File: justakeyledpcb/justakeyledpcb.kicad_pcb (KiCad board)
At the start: 2 copper layers, 85.3 x 46 mm, 17 parts, among them SW1 SW_Push, SW2 SW_Push, SW3 SW_Push, SW4 SW_Push, U1 XIAO-RP2040-DIP

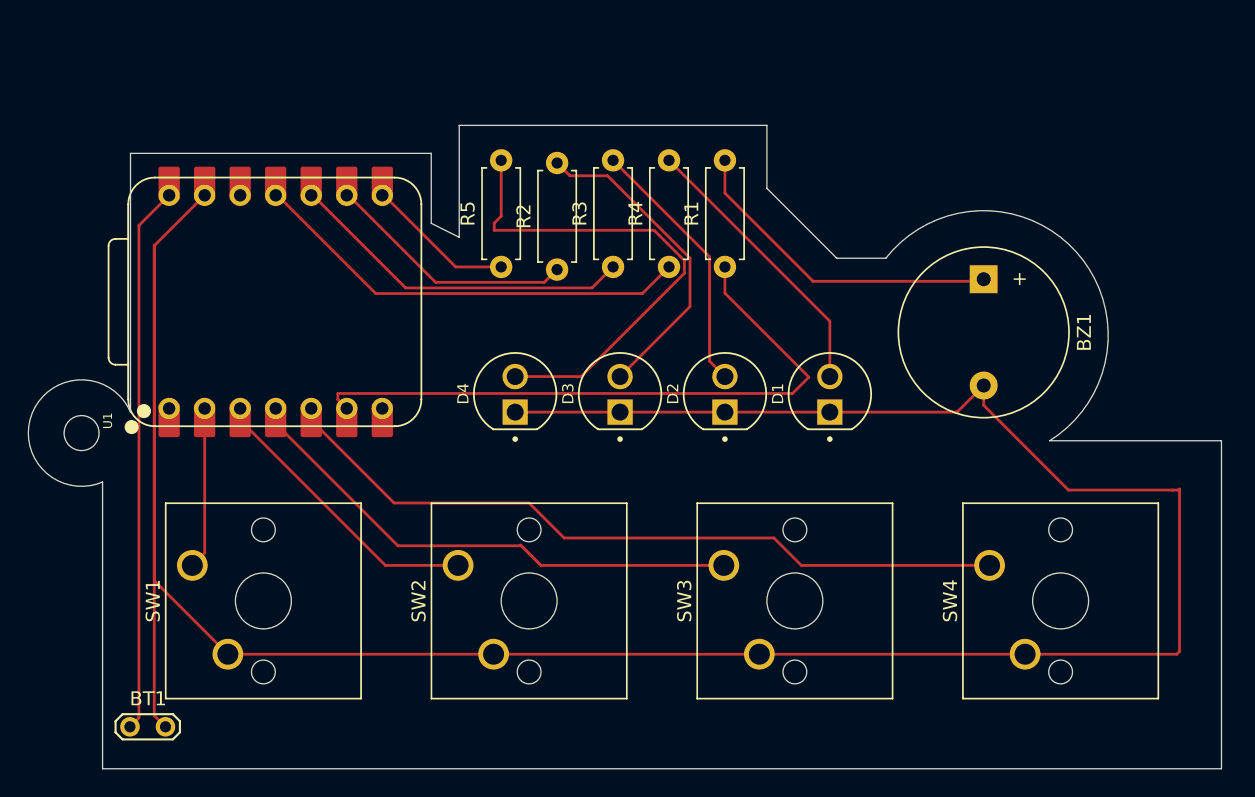
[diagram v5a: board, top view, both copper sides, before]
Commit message: Updated the Shape of the PCB
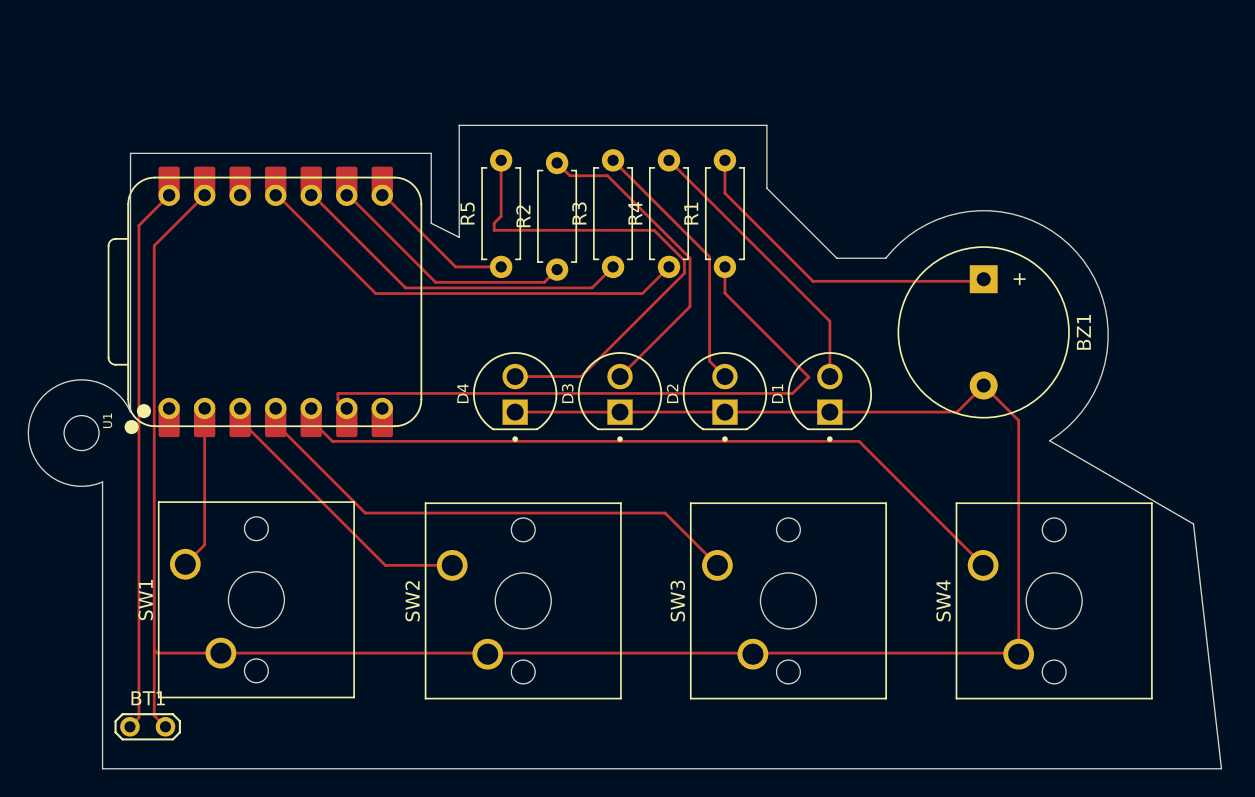
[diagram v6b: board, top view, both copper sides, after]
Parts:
- moved SW1 0.51 mm to (104.4, 70.4)
- moved SW3 0.46 mm to (142.5, 70.5)
- moved SW4 0.46 mm to (161.5, 70.5)
- moved SW2 0.42 mm to (123.5, 70.5)
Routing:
- net GND: track 203.2 -> 156.3 mm
- net Button 3: track 39.4 -> 36.9 mm
- net Button 1: track 12.4 -> 11.7 mm
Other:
- outline, holes or cut-outs redrawn
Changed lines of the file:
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@@
 	(footprint "Button_Switch_Keyboard:SW_Cherry_MX_1.00u_PCB"
 		(layer "F.Cu")
-		(at 142.92 70.46 90)
+		(at 142.46 70.46 90)
 		(descr "Cherry MX keyswitch, 1.00u, PCB mount, http://cherryamericas.com/wp-content/uploads/2014/12/mx_cat.pdf")
 		(tags "Cherry MX keyswitch 1.00u PCB")
@@
 	(footprint "Button_Switch_Keyboard:SW_Cherry_MX_1.00u_PCB"
 		(layer "F.Cu")
-		(at 123.92 70.46 90)
+		(at 123.5 70.46 90)
 		(descr "Cherry MX keyswitch, 1.00u, PCB mount, http://cherryamericas.com/wp-content/uploads/2014/12/mx_cat.pdf")
 		(tags "Cherry MX keyswitch 1.00u PCB")
@@
 	(footprint "Button_Switch_Keyboard:SW_Cherry_MX_1.00u_PCB"
 		(layer "F.Cu")
-		(at 104.92 70.46 90)
+		(at 104.42 70.38 90)
 		(descr "Cherry MX keyswitch, 1.00u, PCB mount, http://cherryamericas.com/wp-content/uploads/2014/12/mx_cat.pdf")
 		(tags "Cherry MX keyswitch 1.00u PCB")
@@
 	(footprint "Button_Switch_Keyboard:SW_Cherry_MX_1.00u_PCB"
 		(layer "F.Cu")
-		(at 161.92 70.46 90)
+		(at 161.46 70.46 90)
 		(descr "Cherry MX keyswitch, 1.00u, PCB mount, http://cherryamericas.com/wp-content/uploads/2014/12/mx_cat.pdf")
 		(tags "Cherry MX keyswitch 1.00u PCB")
@@
 	)
 	(gr_line
-		(start 166.21818 61.54909)
-		(end 178.5 61.54909)
-		(stroke
-			(width 0.05)
-			(type default)
-		)
-		(layer "Edge.Cuts")
-	)
-	(gr_line
 		(start 122 46)
 		(end 124 47)
@@
 	)
 	(gr_line
-		(start 178.5 85)
-		(end 98.5 85)
+		(start 166.218181 61.549089)
+		(end 176.5 67.5)
 		(stroke
 			(width 0.05)
@@
 	)
 	(gr_line
-		(start 146 43.5)
-		(end 151 48.5)
+		(start 176.5 67.5)
+		(end 178.5 85)
 		(stroke
 			(width 0.05)
@@
 	)
 	(gr_line
-		(start 100.5 59.500002)
-		(end 100.5 41)
+		(start 178.5 85)
+		(end 98.5 85)
 		(stroke
 			(width 0.05)
@@
 	)
 	(gr_line
-		(start 178.5 85)
-		(end 178.5 61.54909)
+		(start 146 43.5)
+		(end 151 48.5)
+		(stroke
+			(width 0.05)
+			(type default)
+		)
+		(layer "Edge.Cuts")
+	)
+	(gr_line
+		(start 100.5 59.500002)
+		(end 100.5 41)
 		(stroke
 			(width 0.05)
@@
 	)
 	(segment
-		(start 128 59.5)
-		(end 159.6 59.5)
+		(start 102.427 76.73)
+		(end 106.96 76.73)
 		(width 0.2)
 		(layer "F.Cu")
@@
 	)
 	(segment
-		(start 102.197 47.603)
-		(end 102.197 71.547)
-		(width 0.2)
-		(layer "F.Cu")
-		(net 2)
-	)
-	(segment
-		(start 102.197 47.603)
-		(end 105.8 44)
-		(width 0.2)
-		(layer "F.Cu")
-		(net 2)
-	)
-	(segment
-		(start 161.5 57.6)
-		(end 161.5 59.014213)
+		(start 128 59.5)
+		(end 159.6 59.5)
 		(width 0.2)
 		(layer "F.Cu")
@@
 	)
 	(segment
-		(start 159.6 59.5)
-		(end 161.5 57.6)
+		(start 164 76.81)
+		(end 164 60.1)
 		(width 0.2)
 		(layer "F.Cu")
@@
 	)
 	(segment
-		(start 175 65.075)
-		(end 175.425 65.075)
+		(start 163.92 76.73)
+		(end 164 76.81)
 		(width 0.2)
 		(layer "F.Cu")
@@
 	)
 	(segment
-		(start 175.425 65.075)
-		(end 175.5 65)
+		(start 102.197 47.603)
+		(end 105.8 44)
 		(width 0.2)
 		(layer "F.Cu")
@@
 	)
 	(segment
-		(start 167.560787 65.075)
-		(end 175 65.075)
+		(start 102.197 81.197)
+		(end 103 82)
 		(width 0.2)
 		(layer "F.Cu")
@@
 	)
 	(segment
-		(start 175.31 76.81)
-		(end 164.46 76.81)
+		(start 159.6 59.5)
+		(end 161.5 57.6)
 		(width 0.2)
 		(layer "F.Cu")
@@
 	)
 	(segment
-		(start 175.5 76.62)
-		(end 175.31 76.81)
+		(start 102.197 47.603)
+		(end 102.197 76.5)
 		(width 0.2)
 		(layer "F.Cu")
@@
 	)
 	(segment
-		(start 102.197 81.197)
-		(end 102.197 47.603)
+		(start 102.197 76.5)
+		(end 102.427 76.73)
 		(width 0.2)
 		(layer "F.Cu")
@@
 	)
 	(segment
-		(start 103 82)
+		(start 102.197 76.5)
 		(end 102.197 81.197)
 		(width 0.2)
@@
 	)
 	(segment
-		(start 175.5 65)
-		(end 175.5 76.62)
-		(width 0.2)
-		(layer "F.Cu")
-		(net 2)
-	)
-	(segment
-		(start 102.197 71.547)
-		(end 107.46 76.81)
-		(width 0.2)
-		(layer "F.Cu")
-		(net 2)
-	)
-	(segment
-		(start 107.46 76.81)
-		(end 164.46 76.81)
+		(start 164 60.1)
+		(end 161.5 57.6)
 		(width 0.2)
 		(layer "F.Cu")
@@
 	)
 	(segment
-		(start 161.5 59.014213)
-		(end 167.560787 65.075)
+		(start 106.96 76.73)
+		(end 163.92 76.73)
 		(width 0.2)
 		(layer "F.Cu")
@@
 	)
 	(segment
-		(start 105.8 69.58)
-		(end 104.92 70.46)
+		(start 105.8 60.075)
+		(end 105.8 59.24)
 		(width 0.2)
 		(layer "F.Cu")
@@
 	(segment
 		(start 105.8 60.075)
-		(end 105.8 59.24)
+		(end 105.8 69)
 		(width 0.2)
 		(layer "F.Cu")
@@
 	)
 	(segment
-		(start 105.8 59.24)
-		(end 105.8 69.58)
+		(start 105.8 69)
+		(end 104.42 70.38)
 		(width 0.2)
 		(layer "F.Cu")
@@
 	)
 	(segment
-		(start 108.34 60.075)
-		(end 118.725 70.46)
+		(start 118.725 70.46)
+		(end 123.5 70.46)
 		(width 0.2)
 		(layer "F.Cu")
@@
 	)
 	(segment
-		(start 118.725 70.46)
-		(end 123.92 70.46)
+		(start 108.34 60.075)
+		(end 118.725 70.46)
 		(width 0.2)
 		(layer "F.Cu")
@@
 	)
 	(segment
-		(start 119.62137 69.059)
-		(end 128.44053 69.059)
+		(start 117.28137 66.719)
+		(end 138.719 66.719)
 		(width 0.2)
 		(layer "F.Cu")
@@
 	)
 	(segment
-		(start 128.44053 69.059)
-		(end 129.84153 70.46)
+		(start 110.88 60.31763)
+		(end 117.28137 66.719)
 		(width 0.2)
 		(layer "F.Cu")
@@
 	)
 	(segment
-		(start 129.84153 70.46)
-		(end 142.92 70.46)
-		(width 0.2)
-		(layer "F.Cu")
-		(net 14)
-	)
-	(segment
-		(start 110.88 60.31763)
-		(end 119.62137 69.059)
-		(width 0.2)
-		(layer "F.Cu")
-		(net 14)
-	)
-	(segment
-		(start 128.38153 69)
-		(end 129.84153 70.46)
+		(start 138.719 66.719)
+		(end 142.46 70.46)
 		(width 0.2)
 		(layer "F.Cu")
@@
 	(segment
 		(start 113.42 60.075)
-		(end 119.345 66)
-		(width 0.2)
-		(layer "F.Cu")
-		(net 15)
-	)
-	(segment
-		(start 119.345 66)
-		(end 129 66)
-		(width 0.2)
-		(layer "F.Cu")
-		(net 15)
-	)
-	(segment
-		(start 148.46 70.46)
-		(end 161.92 70.46)
-		(width 0.2)
-		(layer "F.Cu")
-		(net 15)
-	)
-	(segment
-		(start 129 66)
-		(end 131.5 68.5)
+		(end 114.937 61.592)
 		(width 0.2)
 		(layer "F.Cu")
@@
 	)
 	(segment
-		(start 131.5 68.5)
-		(end 146.5 68.5)
+		(start 114.937 61.592)
+		(end 152.592 61.592)
 		(width 0.2)
 		(layer "F.Cu")
@@
 	)
 	(segment
-		(start 146.5 68.5)
-		(end 148.46 70.46)
+		(start 152.592 61.592)
+		(end 161.46 70.46)
 		(width 0.2)
 		(layer "F.Cu")

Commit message: had fun with the beizure curve thingy
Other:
- board size 85.3 x 46 mm -> 85.7 x 52.9 mm
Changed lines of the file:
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@@
 	)
 	(gr_line
-		(start 146 39)
-		(end 146 43.5)
-		(stroke
-			(width 0.05)
-			(type default)
-		)
-		(layer "Edge.Cuts")
-	)
-	(gr_line
-		(start 124 47)
-		(end 124 39)
+		(start 166.21818 61.54909)
+		(end 174.5 61.54909)
 		(stroke
 			(width 0.05)
@@
 	)
 	(gr_line
-		(start 100.5 41)
-		(end 122 41)
-		(stroke
-			(width 0.05)
-			(type default)
-		)
-		(layer "Edge.Cuts")
-	)
-	(gr_line
 		(start 98.5 64.499999)
 		(end 98.5 85)
@@
 	)
 	(gr_line
-		(start 124 39)
-		(end 146 39)
+		(start 98.5 85)
+		(end 172.5 85)
 		(stroke
 			(width 0.05)
@@
 		(layer "Edge.Cuts")
 	)
-	(gr_line
-		(start 166.218181 61.549089)
-		(end 176.5 67.5)
+	(gr_curve
+		(pts
+			(xy 174.5 61.54909) (xy 178.5 61.54909) (xy 178.5 66.5) (xy 178.5 66.5)
+		)
 		(stroke
 			(width 0.05)
@@
 		(layer "Edge.Cuts")
 	)
-	(gr_line
-		(start 176.5 67.5)
-		(end 178.5 85)
-		(stroke
-			(width 0.05)
-			(type default)
+	(gr_curve
+		(pts
+			(xy 124 47) (xy 128.5 12.5) (xy 151 48.5) (xy 151 48.5)
 		)
-		(layer "Edge.Cuts")
-	)
-	(gr_line
-		(start 178.5 85)
-		(end 98.5 85)
-		(stroke
-			(width 0.05)
-			(type default)
-		)
-		(layer "Edge.Cuts")
-	)
-	(gr_line
-		(start 146 43.5)
-		(end 151 48.5)
 		(stroke
 			(width 0.05)
@@
 		(stroke
 			(width 0.05)
+			(type default)
+		)
+		(layer "Edge.Cuts")
+	)
+	(gr_curve
+		(pts
+			(xy 100.5 41) (xy 81.5 37.5) (xy 122 30) (xy 122 41)
+		)
+		(stroke
+			(width 0.05)
+			(type default)
+		)
+		(layer "Edge.Cuts")
+	)
+	(gr_curve
+		(pts
+			(xy 172.5 85) (xy 181 85) (xy 178.5 66.5) (xy 178.5 66.5)
+		)
+		(stroke
+			(width 0.05)

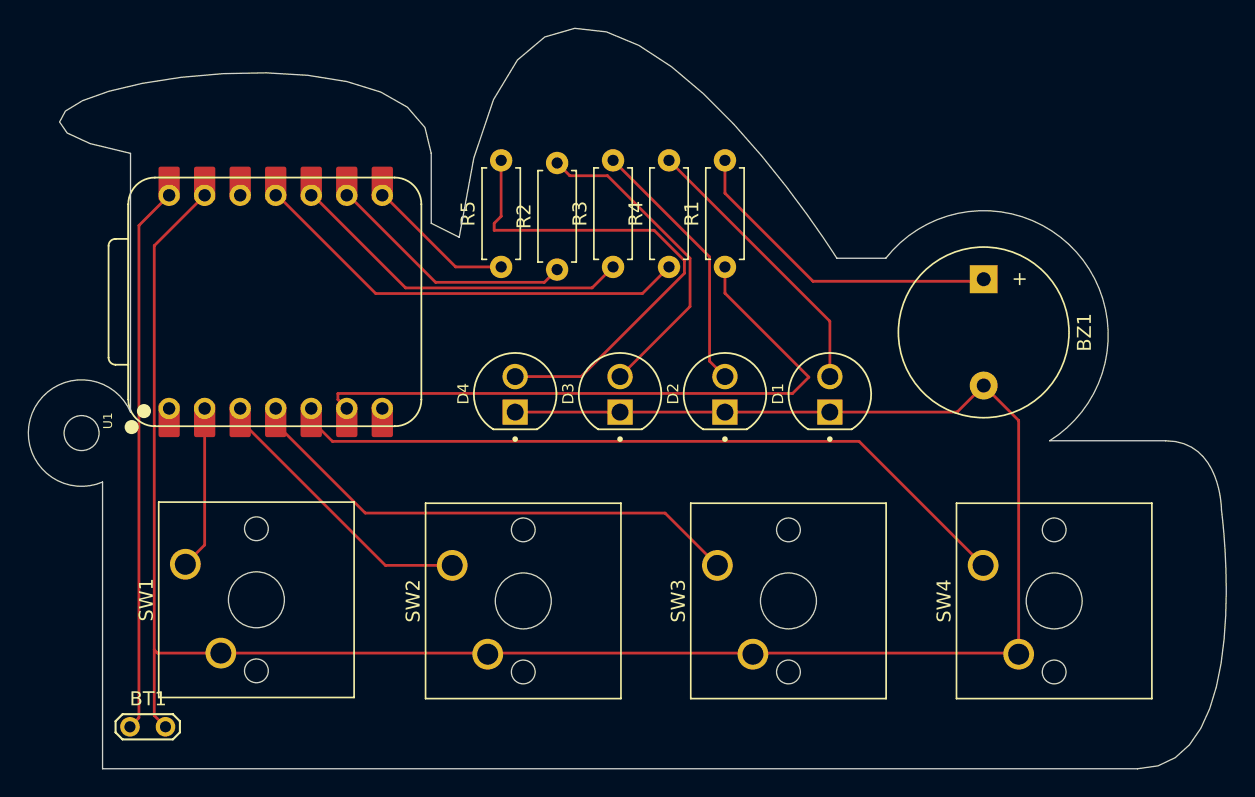
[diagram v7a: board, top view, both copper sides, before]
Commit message: added the silkscreen
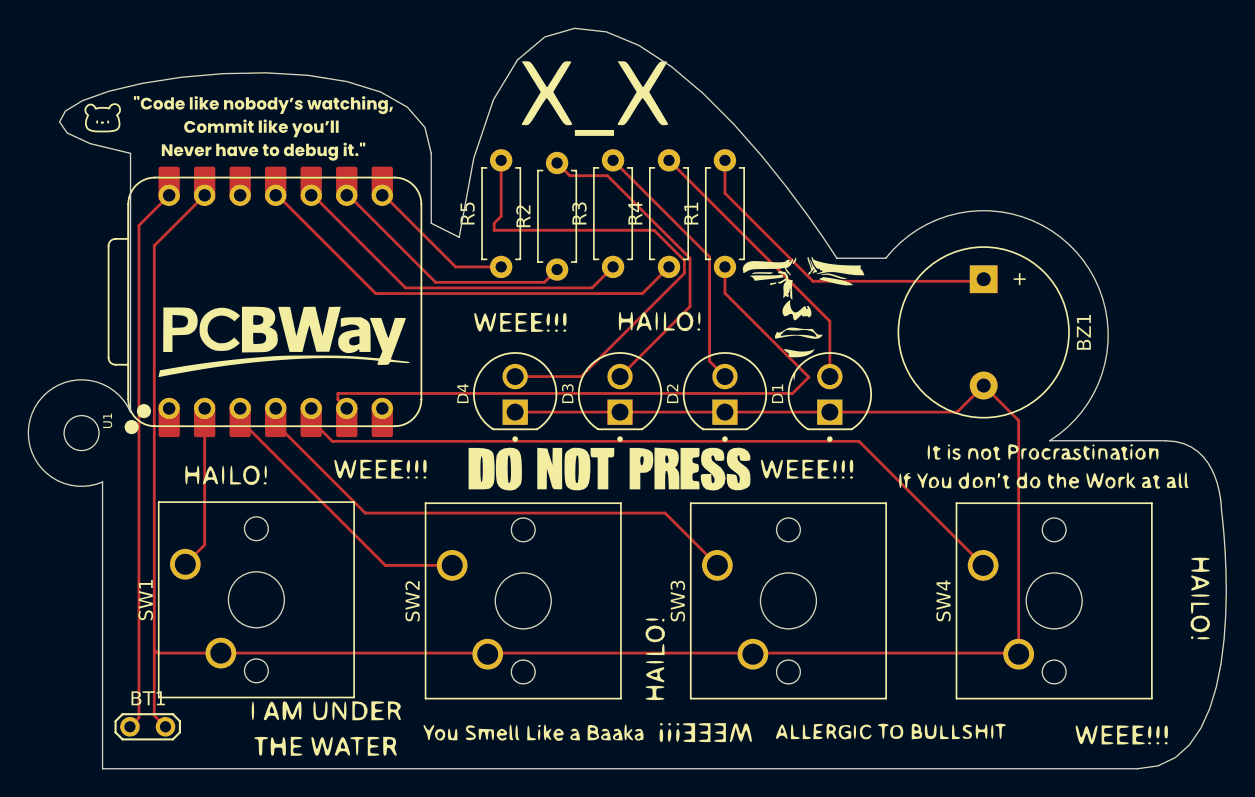
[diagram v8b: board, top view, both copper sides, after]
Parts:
- added G***: LOGO, LOGO, F.Cu at (128.5, 53.0)
- added G***: LOGO, LOGO, F.Cu at (118.5, 63.5)
- added G***: LOGO, LOGO, F.Cu at (177.0, 73.0)
- added G***: LOGO, LOGO, F.Cu at (107.5, 64.0)
- added G***: LOGO, LOGO, F.Cu at (149.0, 63.5)
- added G***: LOGO, LOGO, F.Cu at (155.0, 82.5)
- added G***: LOGO, LOGO, F.Cu at (138.5, 53.0)
- added G***: LOGO, LOGO, F.Cu at (171.5, 82.5)
- added G***: LOGO, LOGO, F.Cu at (129.5, 82.5)
- added G***: LOGO, LOGO, F.Cu at (138.0, 77.0)
- added G***: LOGO, LOGO, F.Cu at (166.0, 63.5)
- added G***: LOGO, LOGO, F.Cu at (133.5, 37.0)
- added G***: LOGO, LOGO, B.Cu at (135.0, 45.5)
- added G***: LOGO, LOGO, B.Cu at (173.5, 73.0)
- added G***: LOGO, LOGO, B.Cu at (113.0, 52.0)
- added G***: LOGO, LOGO, B.Cu at (138.5, 64.5)
- added G***: LOGO, LOGO, B.Cu at (112.0, 47.5)
- added G***: LOGO, LOGO, B.Cu at (113.0, 56.0)
- added G***: LOGO, LOGO, B.Cu at (117.5, 79.0)
- added G***: LOGO, LOGO, B.Cu at (109.0, 38.5)
- added G***: LOGO, LOGO, B.Cu at (157.5, 64.0)
- added G***: LOGO, LOGO, B.Cu at (161.0, 81.5)
- added G***: LOGO, LOGO, F.Cu at (98.5, 38.5)
- added G***: LOGO, LOGO, F.Cu at (114.5, 82.0)
- added G***: LOGO, LOGO, F.Cu at (135.0, 63.5)
- added G***: LOGO, LOGO, F.Cu at (148.5, 52.5)
- added G***: LOGO, LOGO, F.Cu at (111.5, 54.5)
- added G***: LOGO, LOGO, F.Cu at (141.5, 82.5)
- added G***: LOGO, LOGO, F.Cu at (110.0, 38.5)
